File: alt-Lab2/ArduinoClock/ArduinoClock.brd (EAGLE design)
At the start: 54.2 x 17.8 mm, 37 parts, among them IC1 DS3231/SO, U1 MIC5225-5.0, U2 ATMEGA328P, U3 CP2104, U4 MIC5225-3.3, X1 20329, Y2 CSTCE16M0V53-R0 16MHZ

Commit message: passed design checks!
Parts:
- moved C4 1.27 mm to (28.1, 5.69), turned to 90 degrees
- turned R8 to 180 degrees
- turned RESET to 90 degrees
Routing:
- net VBAT: track 7.50 -> 12.9 mm
- net AREF: track 11.8 -> 15.7 mm
- net RESET: track 54.4 -> 56.9 mm, vias 2 -> 3
- net VCCIO: track 59.6 -> 57.2 mm
- net 3.3V: track 91.1 -> 93.3 mm
- net IO3: track 15.9 -> 14.3 mm
- net AD5/SCL: track 36.5 -> 35.2 mm
- net IO0: track 17.7 -> 16.6 mm
- net GND: track 46.0 -> 47.1 mm
- net TXD: track 44.2 -> 43.2 mm
- net N$2: track 0.89 -> 0.00 mm
- net IO2: track 15.1 -> 14.4 mm
- net IO4: track 12.3 -> 12.9 mm

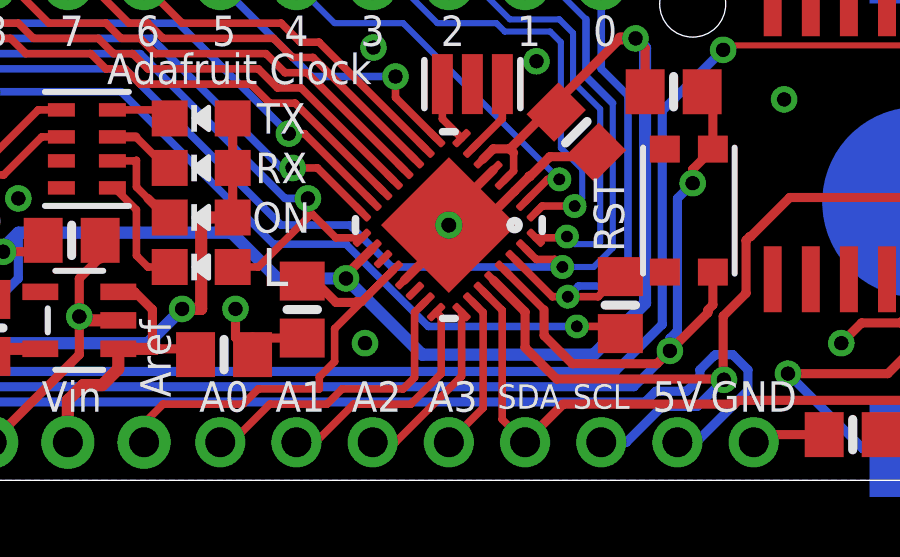
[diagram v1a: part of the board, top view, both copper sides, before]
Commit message: fixed problems with placement.
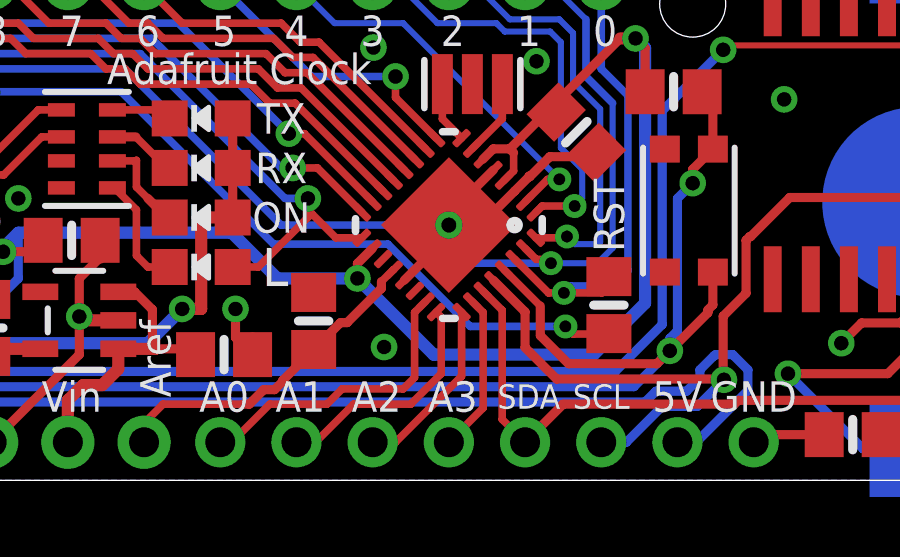
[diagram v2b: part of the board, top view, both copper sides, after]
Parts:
- moved C4 0.54 mm to (28.5, 5.31), turned to 270 degrees
- moved R11 0.38 mm to (38.4, 5.84)
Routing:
- net AREF: track 15.7 -> 11.5 mm
- net GND: track 47.1 -> 45.5 mm
- net TXD: track 43.2 -> 42.6 mm
